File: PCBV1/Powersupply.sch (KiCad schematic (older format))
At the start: 49 parts, among them J2 Conn_WallPlug, T1 EFD 20/10/7, U1 ST1S41PHR, U2 ST1S41PHR, U3 VIPER318HDTR

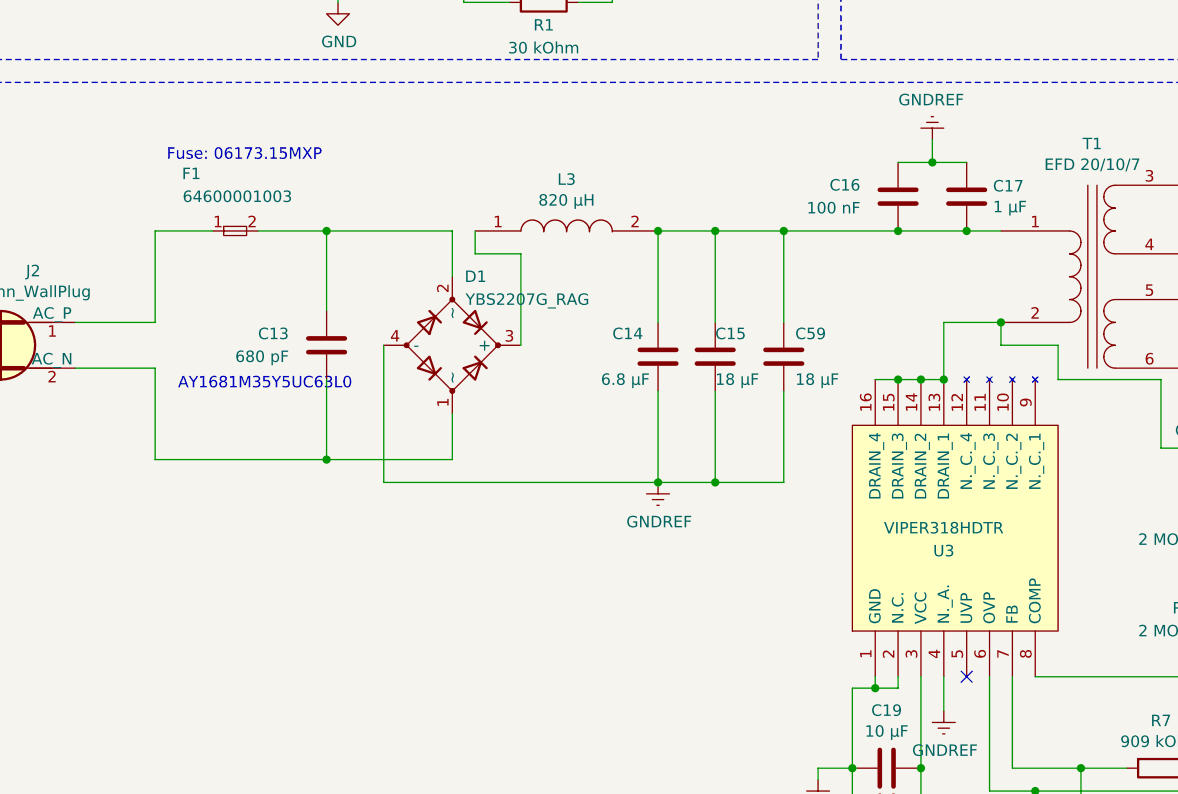
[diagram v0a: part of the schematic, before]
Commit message: Added new JTAG/UART header with connections for STLink V3. Moved from SamacSys to personal GitHub-based library.
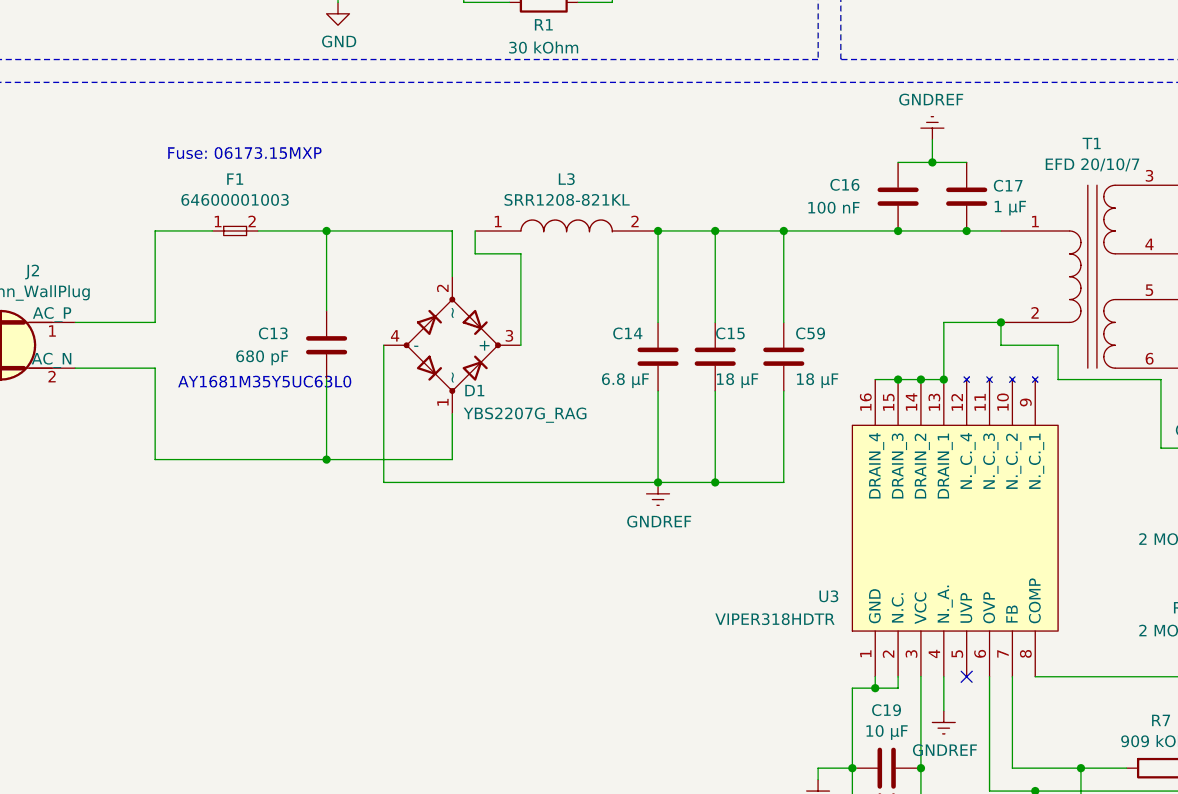
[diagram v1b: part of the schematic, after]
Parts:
- removed D1: YBS2207G_RAG, YBS2207GRAG, symbol SamacSys_Parts:YBS2207G_RAG
- removed F1: 64600001003, 646-SERIESHOLDER, symbol SamacSys_Parts:64600001003
- removed L1: SRN6045TA-101M, SRN6045TA220M, symbol SamacSys_Parts:SRN6045TA-101M
- removed L3: 820 µH, INDPM127127X850N, symbol SamacSys_Parts:SRR1208-821KL
- removed U1, U2: ST1S41PHR, SOIC127P600X170-9N, symbol Regulator_Switching:ST1S41PHR
- removed U3: VIPER318HDTR, SOIC127P600X175-16N, symbol SamacSys_Parts:VIPER318HDTR
- added D1: YBS2207G_RAG, Personal_Passives:YBS2207G_RAG, symbol Personal_Passives:YBS2207G_RAG
- added F1: 64600001003, Personal_Misc:64600001003, symbol Personal_Misc:64600001003
- added L1: SRN6045TA-101M, Personal_Passives:SRN6045TA-101M, symbol Personal_Passives:SRN6045TA-101M
- added L3: SRR1208-821KL, Personal_Passives:SRR1208-821KL, symbol Personal_Passives:SRR1208-821KL
- added U1, U2: ST1S41PHR, Personal_ICs:ST1S41PHR, symbol Personal_ICs:ST1S41PHR
- added U3: VIPER318HDTR, Personal_ICs:VIPER318HDTR, symbol Personal_ICs:VIPER318HDTR
- T1: footprint SamacSys_Parts:B66418W1008D1 -> Personal_Misc:EFD_20_10_7
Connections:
- net 12V: now also U1.1 (VINA), U1.2 (EN), U1.6 (VINSW), U2.1 (VINA), U2.2 (EN), U2.6 (VINSW)
- net 3V3: now also L1.2
- net GND: now also U1.4 (GND), U1.5 (NC), U1.8 (PGND), U1.9 (EPAD), U2.4 (GND), U2.5 (NC), U2.8 (PGND), U2.9 (EPAD)
- net GNDREF: now also D1.4 (-), U3.1 (GND), U3.2 (N.C.), U3.4 (N._A.)
- net at C5.2, R1.2, R2.1: now also U1.3 (FB)
- net at L2.1: now also U2.7 (SW)
- net at C11.2, R3.2, R4.1: now also U2.3 (FB)
- net at J2.1 (AC_P): now also F1.1
- net at C13.2, J2.2 (AC_N): now also D1.1 (~~)
- net at C13.1: now also D1.2 (~~), F1.2
- net at C18.1, C19.1, D3.1 (K)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: now also U3.3 (VCC)
- net at C14.1, C15.1, C16.2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: now also L3.2
- net at R5.1, T1.2 (AB): now also U3.13 (DRAIN_1), U3.14 (DRAIN_2), U3.15 (DRAIN_3), U3.16 (DRAIN_4)
- net at R25.2, R6.1: now also U3.6 (OVP)
- net at R7.2, R8.1: now also U3.7 (FB)
- net at C21.2, R9.2: now also U3.8 (COMP)
- new net: L1.1, U1.7 (SW)
- new net: D1.3 (+), L3.1
